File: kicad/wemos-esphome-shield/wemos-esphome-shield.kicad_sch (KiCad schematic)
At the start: 16 parts, among them Q1 2N2219, Q2 2N2219, Q3 2N2219, T1 Transformer_1P_1S, U1 WeMos_D1_mini

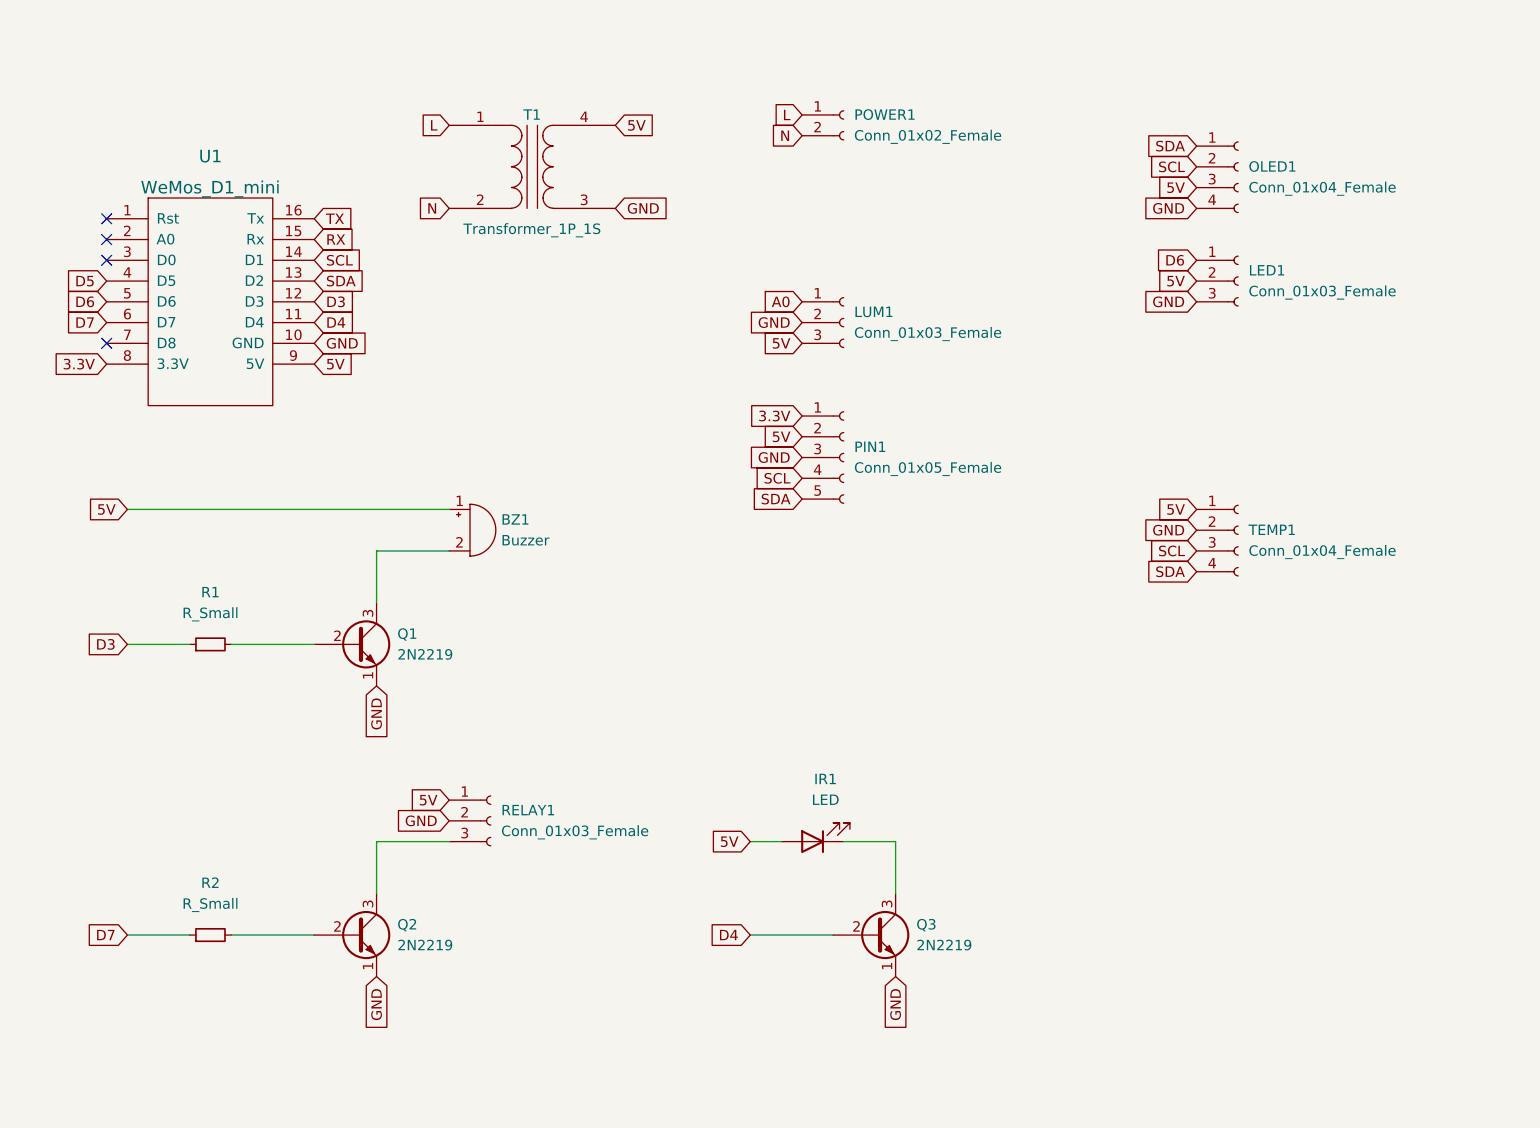
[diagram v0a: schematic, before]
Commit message: fix footprints and schematic
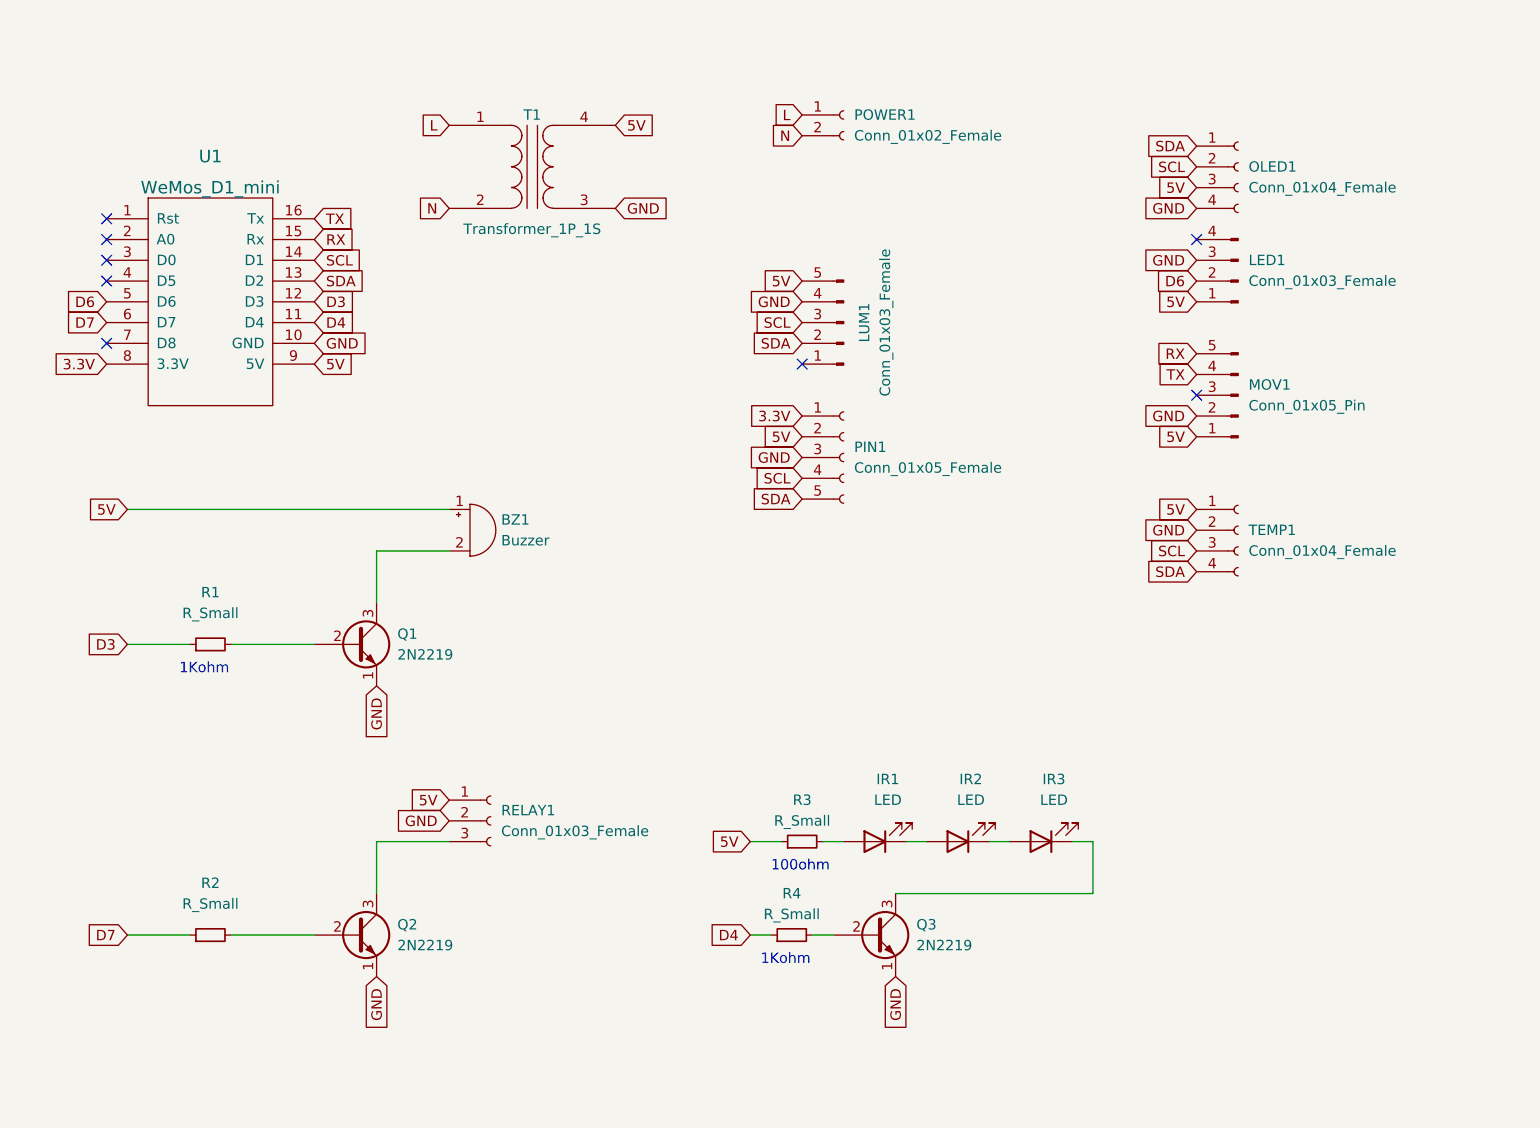
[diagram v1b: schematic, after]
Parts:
- added IR2, IR3: LED, LED_THT:LED_D5.0mm, symbol Device:LED
- added MOV1: Conn_01x05_Pin, symbol Connector:Conn_01x05_Pin
- added R3, R4: R_Small, symbol Device:R_Small
- LED1: symbol Connector:Conn_01x03_Female -> Connector:Conn_01x04_Pin
- LUM1: symbol Connector:Conn_01x03_Female -> Connector:Conn_01x05_Pin
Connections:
- net 5V: now also LED1.1 (Pin_1), LUM1.5 (Pin_5), MOV1.1 (Pin_1), R3.1; no longer IR1.2 (A), LED1.2 (Pin_2), LUM1.3 (Pin_3)
- net D4: now also R4.1; no longer Q3.2 (B)
- net D6: now also LED1.2 (Pin_2); no longer LED1.1 (Pin_1)
- net GND: now also LUM1.4 (Pin_4), MOV1.2 (Pin_2); no longer LUM1.2 (Pin_2)
- net RX: now also MOV1.5 (Pin_5)
- net SCL: now also LUM1.3 (Pin_3)
- net SDA: now also LUM1.2 (Pin_2)
- net TX: now also MOV1.4 (Pin_4)
- net at IR1.1 (K): now also IR2.2 (A); no longer Q3.3 (C)
- net A0: no longer names the net of LUM1.1 (Pin_1)
- net D5: no longer names the net of U1.4 (D5)
- new net: Q3.2 (B), R4.2
- new net: IR1.2 (A), R3.2
- new net: IR3.1 (K), Q3.3 (C)
- new net: IR2.1 (K), IR3.2 (A)
- no-connect marks 4 -> 8
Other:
- note added: "100ohm"
- note added: "1Kohm"
- moved on the sheet: IR1

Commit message: update schematic
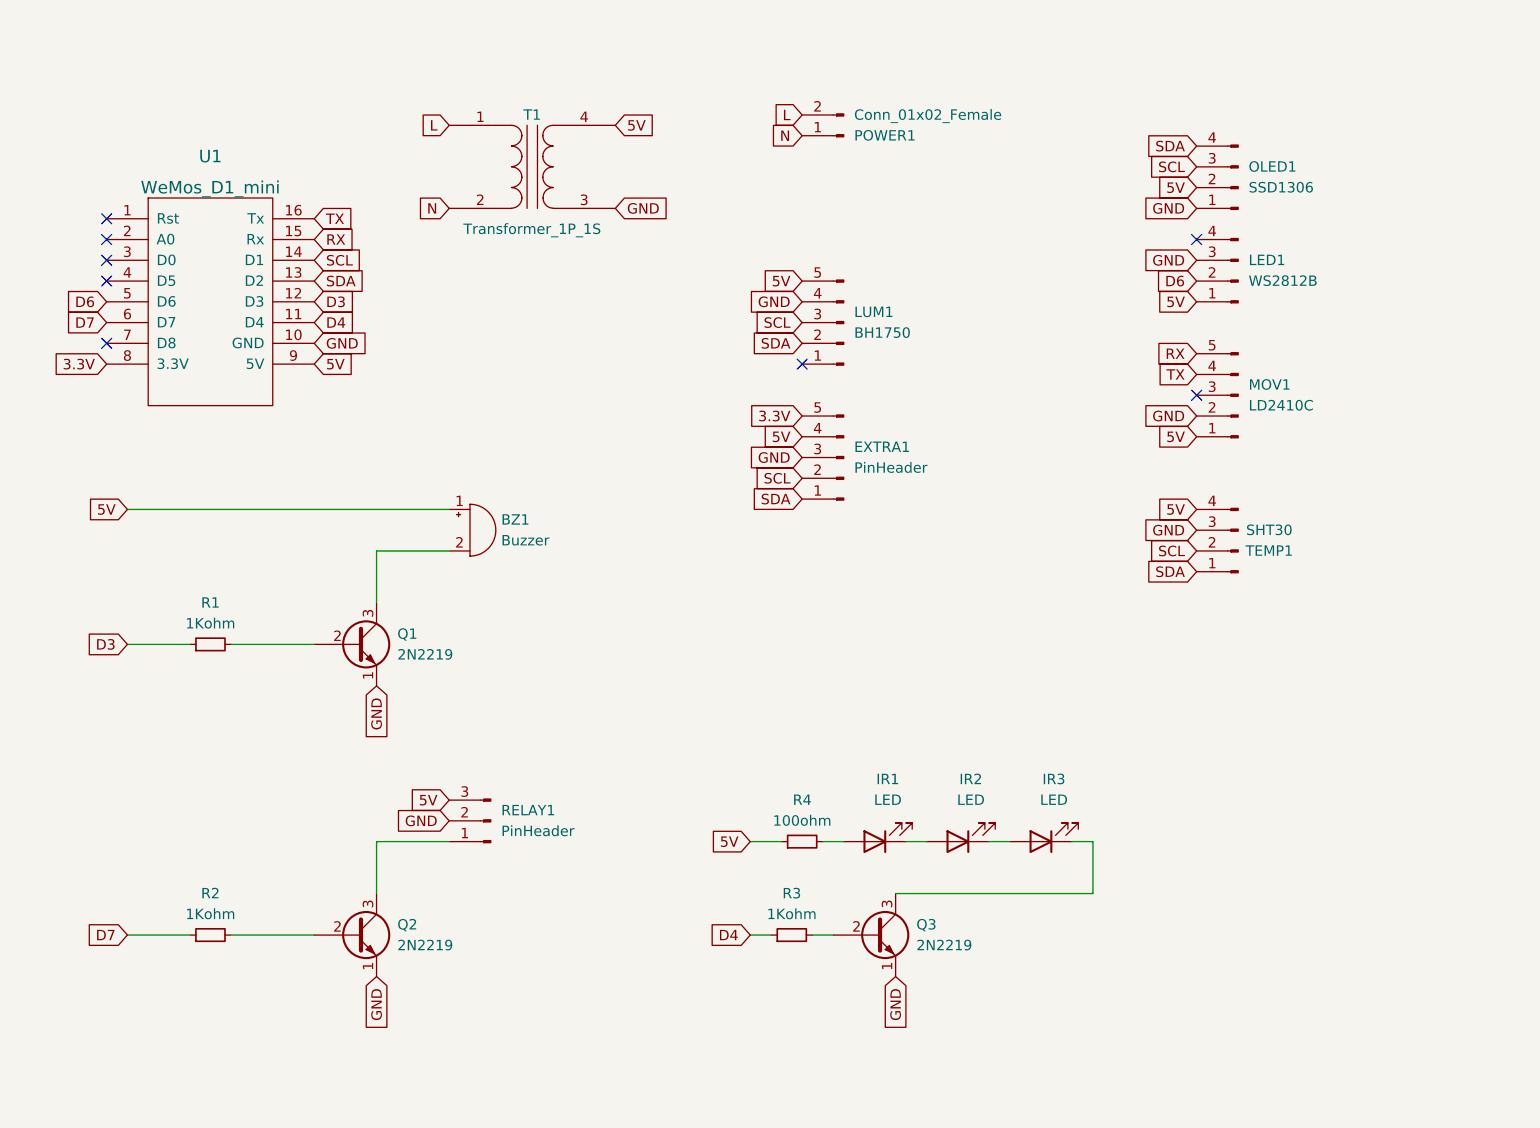
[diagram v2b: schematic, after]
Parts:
- EXTRA1: renamed from PIN1; value Conn_01x05_Female -> PinHeader; symbol Connector:Conn_01x05_Female -> Connector:Conn_01x05_Pin
- LED1: value Conn_01x03_Female -> WS2812B
- LUM1: value Conn_01x03_Female -> BH1750
- MOV1: value Conn_01x05_Pin -> LD2410C
- OLED1: value Conn_01x04_Female -> SSD1306; symbol Connector:Conn_01x04_Female -> Connector:Conn_01x04_Pin
- POWER1: symbol Connector:Conn_01x02_Female -> Connector:Conn_01x02_Pin
- R1, R2: value R_Small -> 1Kohm
- R3: renamed from R4; value R_Small -> 1Kohm
- R4: renamed from R3; value R_Small -> 100ohm
- RELAY1: value Conn_01x03_Female -> PinHeader; symbol Connector:Conn_01x03_Female -> Connector:Conn_01x03_Pin
- TEMP1: value Conn_01x04_Female -> SHT30; symbol Connector:Conn_01x04_Female -> Connector:Conn_01x04_Pin
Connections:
- net 3.3V: now also EXTRA1.5 (Pin_5); no longer EXTRA1.1 (Pin_1)
- net 5V: now also EXTRA1.4 (Pin_4), OLED1.2 (Pin_2), RELAY1.3 (Pin_3), TEMP1.4 (Pin_4); no longer EXTRA1.2 (Pin_2), OLED1.3 (Pin_3), RELAY1.1 (Pin_1), TEMP1.1 (Pin_1)
- net GND: now also OLED1.1 (Pin_1), TEMP1.3 (Pin_3); no longer OLED1.4 (Pin_4), TEMP1.2 (Pin_2)
- net L: now also POWER1.2 (Pin_2); no longer POWER1.1 (Pin_1)
- net N: now also POWER1.1 (Pin_1); no longer POWER1.2 (Pin_2)
- net SCL: now also EXTRA1.2 (Pin_2), OLED1.3 (Pin_3), TEMP1.2 (Pin_2); no longer EXTRA1.4 (Pin_4), OLED1.2 (Pin_2), TEMP1.3 (Pin_3)
- net SDA: now also EXTRA1.1 (Pin_1), OLED1.4 (Pin_4), TEMP1.1 (Pin_1); no longer EXTRA1.5 (Pin_5), OLED1.1 (Pin_1), TEMP1.4 (Pin_4)
- net at Q2.3 (C): now also RELAY1.1 (Pin_1); no longer RELAY1.3 (Pin_3)
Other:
- note removed: "100ohm"
- note removed: "1Kohm"

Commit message: update schematic
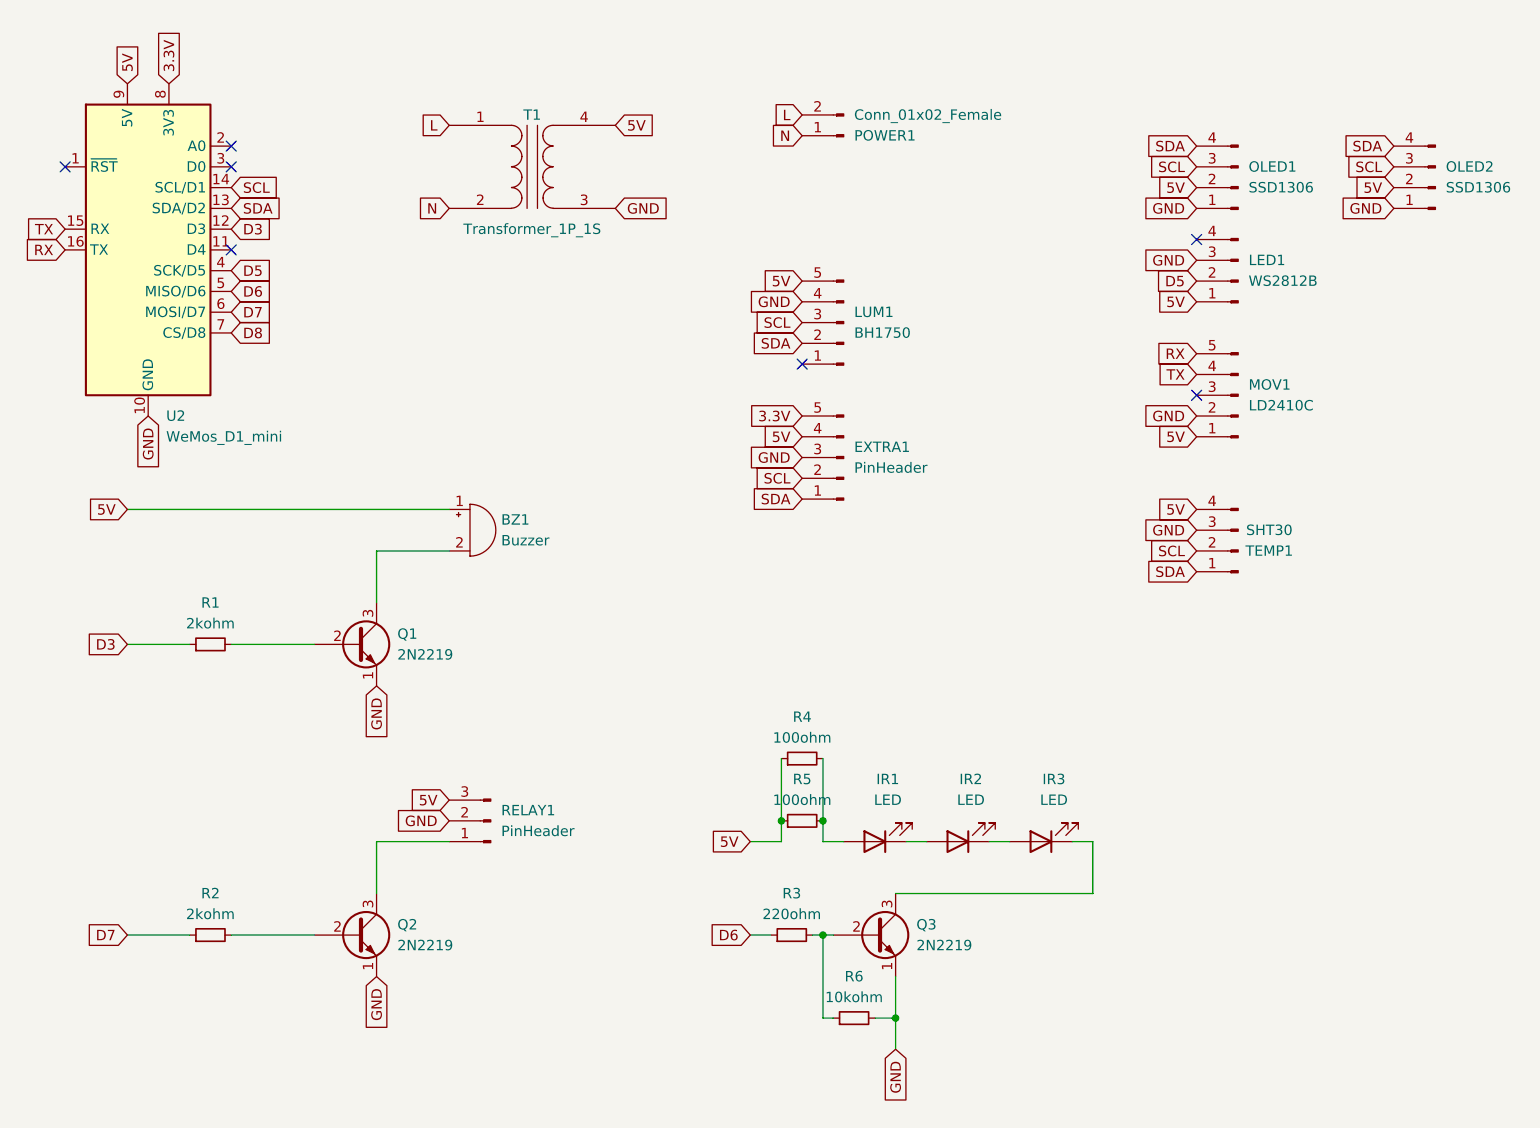
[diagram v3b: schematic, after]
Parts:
- removed U1: WeMos_D1_mini, wemos-d1-mini:wemos-d1-mini-with-pin-header, symbol wemos_mini:WeMos_D1_mini
- added OLED2: SSD1306, internal:SSD1306 OLED 128x32, symbol Connector:Conn_01x04_Pin
- added R5: 100ohm, symbol Device:R_Small
- added R6: 10kohm, symbol Device:R_Small
- added U2: WeMos_D1_mini, Module:WEMOS_D1_mini_light, symbol MCU_Module:WeMos_D1_mini
- R1, R2: value 1Kohm -> 2kohm
- R3: value 1Kohm -> 220ohm
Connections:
- net D4 is gone; now on net D6: R3.1
- net 3.3V: now also U2.8 (3V3)
- net 5V: now also OLED2.2 (Pin_2), R5.1, U2.9 (5V)
- net D3: now also U2.12 (D3)
- net D6: now also U2.5 (MISO/D6); no longer LED1.2 (Pin_2)
- net D7: now also U2.6 (MOSI/D7)
- net GND: now also OLED2.1 (Pin_1), R6.2, U2.10 (GND)
- net RX: now also U2.16 (TX)
- net SCL: now also OLED2.3 (Pin_3), U2.14 (SCL/D1)
- net SDA: now also OLED2.4 (Pin_4), U2.13 (SDA/D2)
- net TX: now also U2.15 (RX)
- net at Q3.2 (B), R3.2: now also R6.1
- net at IR1.2 (A), R4.2: now also R5.2
- new net D5: LED1.2 (Pin_2), U2.4 (SCK/D5)
- new net D8: U2.7 (CS/D8)
- no-connect marks 8 -> 7
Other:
- moved on the sheet: R4

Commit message: update schematics
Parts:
- added GEST1: APDS9960, symbol Connector:Conn_01x06_Pin
- added R2, R7: 10kohm, symbol Device:R_Small
- R6: renamed from R3; value 220ohm -> 2kohm
- renumbered R4 to R3, R5 to R4, R2 to R5, R6 to R8, U2 to U1
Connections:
- net 5V: now also GEST1.3 (Pin_3)
- net GND: now also GEST1.2 (Pin_2), R2.2, R7.2
- net SCL: now also GEST1.5 (Pin_5)
- net SDA: now also GEST1.4 (Pin_4)
- net at Q2.2 (B), R5.2: now also R7.1
- net at Q1.2 (B), R1.2: now also R2.1
- no-connect marks 7 -> 9
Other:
- moved on the sheet: EXTRA1, LED1, LUM1, MOV1, OLED1, OLED2, R3, R4, TEMP1
